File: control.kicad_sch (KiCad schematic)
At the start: 27 parts, among them J1 USB_C_Receptacle_USB2.0, J5 Conn_ARM_JTAG_SWD_10, J7 Conn_01x04_Male, U2 AMS1117-3.3, U3 STM32F042C4Tx

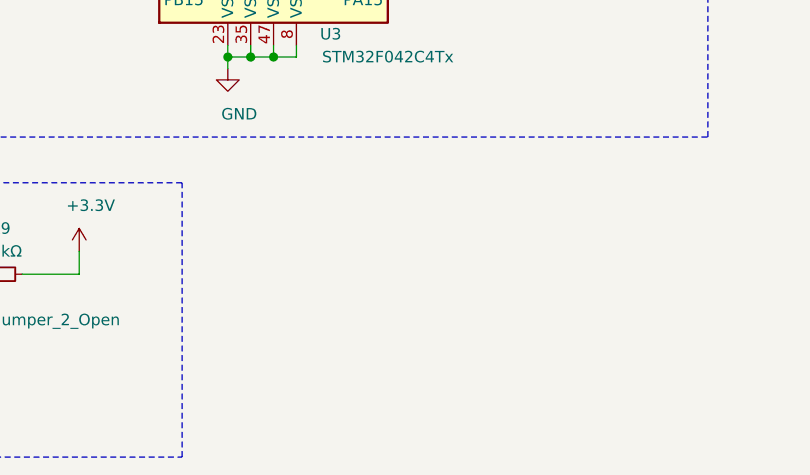
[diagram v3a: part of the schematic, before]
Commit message: fix LEDs, add power LED
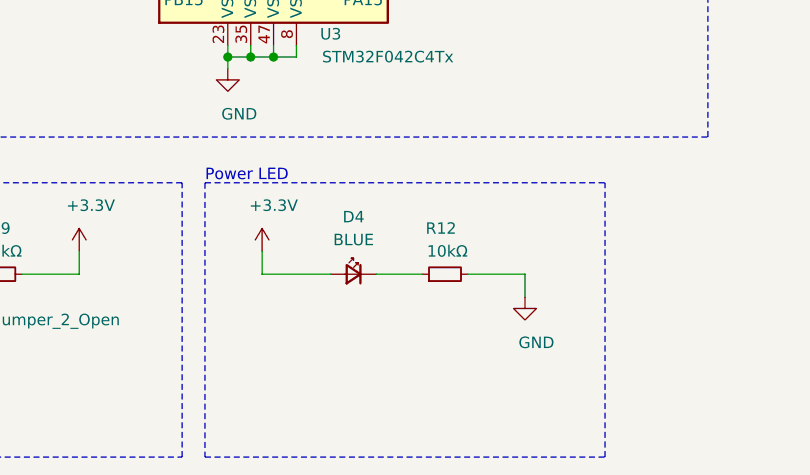
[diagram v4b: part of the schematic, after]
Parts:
- added D4: BLUE, symbol Device:LED_Small
- added R12: 10kΩ, Resistor_SMD:R_0402_1005Metric, symbol Device:R_Small
- J1: footprint (none) -> Connector_USB:USB_C_Receptacle_Amphenol_12401610E4-2A
- L1: footprint (none) -> Inductor_SMD:L_0402_1005Metric
- R1, R2: footprint (none) -> Resistor_SMD:R_0402_1005Metric
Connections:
- net +3V3: now also D4.2 (A)
- net GND: now also R12.2
- new net: D4.1 (K), R12.1
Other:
- note added: "Power LED"
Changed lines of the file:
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@@
+    (stroke (width 0) (type solid) (color 0 0 0 0))
+  )
+  (wire (pts (xy 115.57 170.18) (xy 115.57 172.72))
+    (stroke (width 0) (type solid) (color 0 0 0 0))
+  )
+  (wire (pts (xy 115.57 172.72) (xy 123.19 172.72))
     (stroke (width 0) (type solid) (color 0 0 0 0))
   )
@@
     (stroke (width 0) (type solid) (color 0 0 0 0))
   )
+  (wire (pts (xy 128.27 172.72) (xy 133.35 172.72))
+    (stroke (width 0) (type solid) (color 0 0 0 0))
+  )
   (wire (pts (xy 132.08 31.75) (xy 132.08 34.29))
     (stroke (width 0) (type solid) (color 0 0 0 0))
@@
     (stroke (width 0) (type solid) (color 0 0 0 0))
   )
+  (wire (pts (xy 138.43 172.72) (xy 144.78 172.72))
+    (stroke (width 0) (type solid) (color 0 0 0 0))
+  )
+  (wire (pts (xy 144.78 172.72) (xy 144.78 175.26))
+    (stroke (width 0) (type solid) (color 0 0 0 0))
+  )
   (wire (pts (xy 157.48 26.67) (xy 157.48 29.21))
     (stroke (width 0) (type solid) (color 0 0 0 0))
@@
     (stroke (width 0) (type dash) (color 0 0 0 0))
   )
+  (polyline (pts (xy 109.22 162.56) (xy 109.22 193.04))
+    (stroke (width 0) (type dash) (color 0 0 0 0))
+  )
+  (polyline (pts (xy 109.22 162.56) (xy 153.67 162.56))
+    (stroke (width 0) (type dash) (color 0 0 0 0))
+  )
+  (polyline (pts (xy 109.22 193.04) (xy 153.67 193.04))
+    (stroke (width 0) (type dash) (color 0 0 0 0))
+  )
   (polyline (pts (xy 147.32 17.78) (xy 147.32 52.07))
     (stroke (width 0) (type dash) (color 0 0 0 0))
@@
   )
   (polyline (pts (xy 152.4 50.8) (xy 269.24 50.8))
+    (stroke (width 0) (type dash) (color 0 0 0 0))
+  )
+  (polyline (pts (xy 153.67 193.04) (xy 153.67 162.56))
     (stroke (width 0) (type dash) (color 0 0 0 0))
   )
@@
     (effects (font (size 1.27 1.27)) (justify left bottom))
   )
+  (text "Power LED" (at 109.22 162.56 0)
+    (effects (font (size 1.27 1.27)) (justify left bottom))
+  )
   (text "Power Supply Decoupling" (at 152.4 17.78 0)
     (effects (font (size 1.27 1.27)) (justify left bottom))
@@
     (property "Reference" "L1" (id 0) (at 204.47 59.69 90))
     (property "Value" "39nH" (id 1) (at 204.47 62.23 90))
-    (property "Footprint" "" (id 2) (at 204.47 64.77 0)
+    (property "Footprint" "Inductor_SMD:L_0402_1005Metric" (id 2) (at 204.47 64.77 0)
       (effects (font (size 1.27 1.27)) hide)
     )
@@
     )
   )
+  (symbol (lib_id "power:+3.3V") (at 115.57 170.18 0) (unit 1)
+    (in_bom yes) (on_board yes)
+    (property "Reference" "#PWR032" (id 0) (at 115.57 173.99 0)
+      (effects (font (size 1.27 1.27)) hide)
+    )
+    (property "Value" "+3.3V" (id 1) (at 116.84 165.1 0))
+    (property "Footprint" "" (id 2) (at 115.57 170.18 0)
+      (effects (font (size 1.27 1.27)) hide)
+    )
+    (property "Datasheet" "" (id 3) (at 115.57 170.18 0)
+      (effects (font (size 1.27 1.27)) hide)
+    )
+  )
   (symbol (lib_id "power:+3.3VA") (at 121.92 71.12 0) (unit 1)
     (in_bom yes) (on_board yes)
@@
     )
   )
+  (symbol (lib_id "power:GND") (at 144.78 175.26 0) (unit 1)
+    (in_bom yes) (on_board yes)
+    (property "Reference" "#PWR033" (id 0) (at 144.78 181.61 0)
+      (effects (font (size 1.27 1.27)) hide)
+    )
+    (property "Value" "GND" (id 1) (at 146.05 180.34 0))
+    (property "Footprint" "" (id 2) (at 144.78 175.26 0)
+      (effects (font (size 1.27 1.27)) hide)
+    )
+    (property "Datasheet" "" (id 3) (at 144.78 175.26 0)
+      (effects (font (size 1.27 1.27)) hide)
+    )
+  )
   (symbol (lib_id "power:GND") (at 157.48 41.91 0) (unit 1)
     (in_bom yes) (on_board yes)
@@
       (effects (font (size 1.27 1.27)) (justify left))
     )
-    (property "Footprint" "" (id 2) (at 31.75 86.36 0)
+    (property "Footprint" "Resistor_SMD:R_0402_1005Metric" (id 2) (at 31.75 86.36 0)
       (effects (font (size 1.27 1.27)) hide)
     )
@@
       (effects (font (size 1.27 1.27)) (justify left))
     )
-    (property "Footprint" "" (id 2) (at 50.8 86.36 0)
+    (property "Footprint" "Resistor_SMD:R_0402_1005Metric" (id 2) (at 50.8 86.36 0)
       (effects (font (size 1.27 1.27)) hide)
     )
@@
     )
     (property "Datasheet" "~" (id 3) (at 86.36 172.72 0)
+      (effects (font (size 1.27 1.27)) hide)
+    )
+  )
+  (symbol (lib_id "Device:R_Small") (at 135.89 172.72 90) (unit 1)
+    (in_bom yes) (on_board yes)
+    (property "Reference" "R12" (id 0) (at 137.16 167.64 90)
+      (effects (font (size 1.27 1.27)) (justify left))
+    )
+    (property "Value" "10kΩ" (id 1) (at 138.43 170.18 90)
+      (effects (font (size 1.27 1.27)) (justify left))
+    )
+    (property "Footprint" "Resistor_SMD:R_0402_1005Metric" (id 2) (at 135.89 172.72 0)
+      (effects (font (size 1.27 1.27)) hide)
+    )
+    (property "Datasheet" "~" (id 3) (at 135.89 172.72 0)
       (effects (font (size 1.27 1.27)) hide)
     )
@@
     )
   )
+  (symbol (lib_id "Device:LED_Small") (at 125.73 172.72 0) (mirror y) (unit 1)
+    (in_bom yes) (on_board yes)
+    (property "Reference" "D4" (id 0) (at 125.73 166.37 0))
+    (property "Value" "BLUE" (id 1) (at 125.73 168.91 0))
+    (property "Footprint" "" (id 2) (at 125.73 172.72 90)
+      (effects (font (size 1.27 1.27)) hide)
+    )
+    (property "Datasheet" "~" (id 3) (at 125.73 172.72 90)
+      (effects (font (size 1.27 1.27)) hide)
+    )
+  )
   (symbol (lib_id "Device:C_Small") (at 106.68 36.83 0) (unit 1)
     (in_bom yes) (on_board yes)
@@
     (property "Reference" "J1" (id 0) (at 35.56 21.59 0))
     (property "Value" "USB_C_Receptacle_USB2.0" (id 1) (at 35.56 24.13 0))
-    (property "Footprint" "" (id 2) (at 35.56 44.45 0)
-      (effects (font (size 1.27 1.27)) hide)
-    )
+    (property "Footprint" "Connector_USB:USB_C_Receptacle_Amphenol_12401610E4-2A" (id 2) (at 35.56 44.45 0)
+      (effects (font (size 1.27 1.27)) hide)
+    )

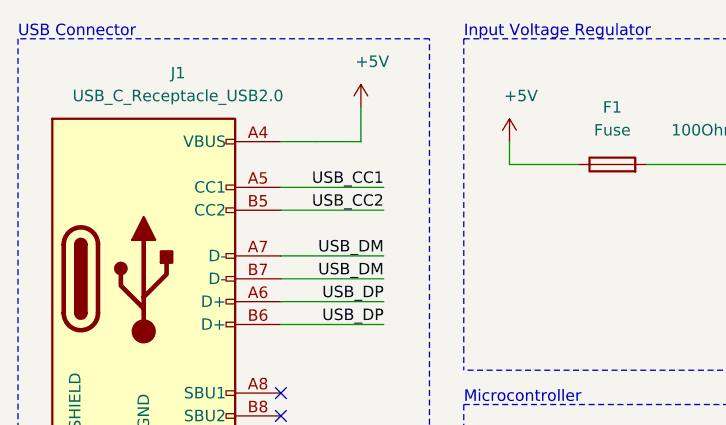
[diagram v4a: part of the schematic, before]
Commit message: add voltage measurement
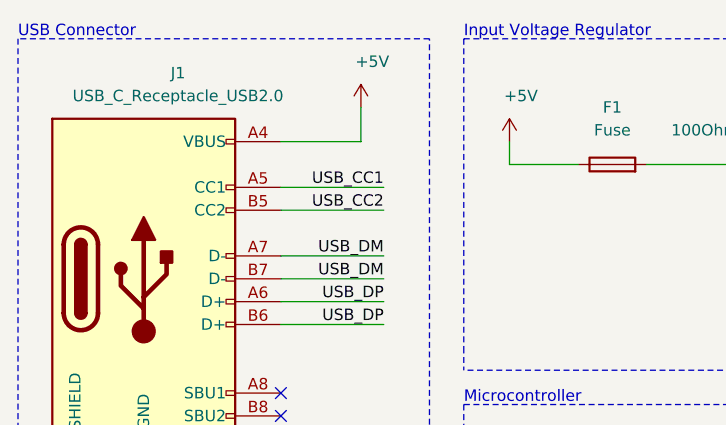
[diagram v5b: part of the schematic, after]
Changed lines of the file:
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@@
   (junction (at 227.33 29.21) (diameter 1.016) (color 0 0 0 0))
   (junction (at 227.33 39.37) (diameter 1.016) (color 0 0 0 0))
-  (no_connect (at 46.99 57.15))
   (no_connect (at 46.99 59.69))
   (no_connect (at 24.13 67.31))
+  (no_connect (at 46.99 57.15))
   (wire (pts (xy 22.86 81.28) (xy 31.75 81.28))
     (stroke (width 0) (type solid) (color 0 0 0 0))
@@
     (stroke (width 0) (type solid) (color 0 0 0 0))
   )
+  (wire (pts (xy 46.99 29.21) (xy 55.88 29.21))
+    (stroke (width 0) (type solid) (color 0 0 0 0))
+  )
   (wire (pts (xy 46.99 34.29) (xy 58.42 34.29))
     (stroke (width 0) (type solid) (color 0 0 0 0))
@@
     (stroke (width 0) (type solid) (color 0 0 0 0))
   )
-  (wire (pts (xy 50.8 29.21) (xy 46.99 29.21))
-    (stroke (width 0) (type solid) (color 0 0 0 0))
-  )
-  (wire (pts (xy 50.8 29.21) (xy 55.88 29.21))
-    (stroke (width 0) (type solid) (color 0 0 0 0))
-  )

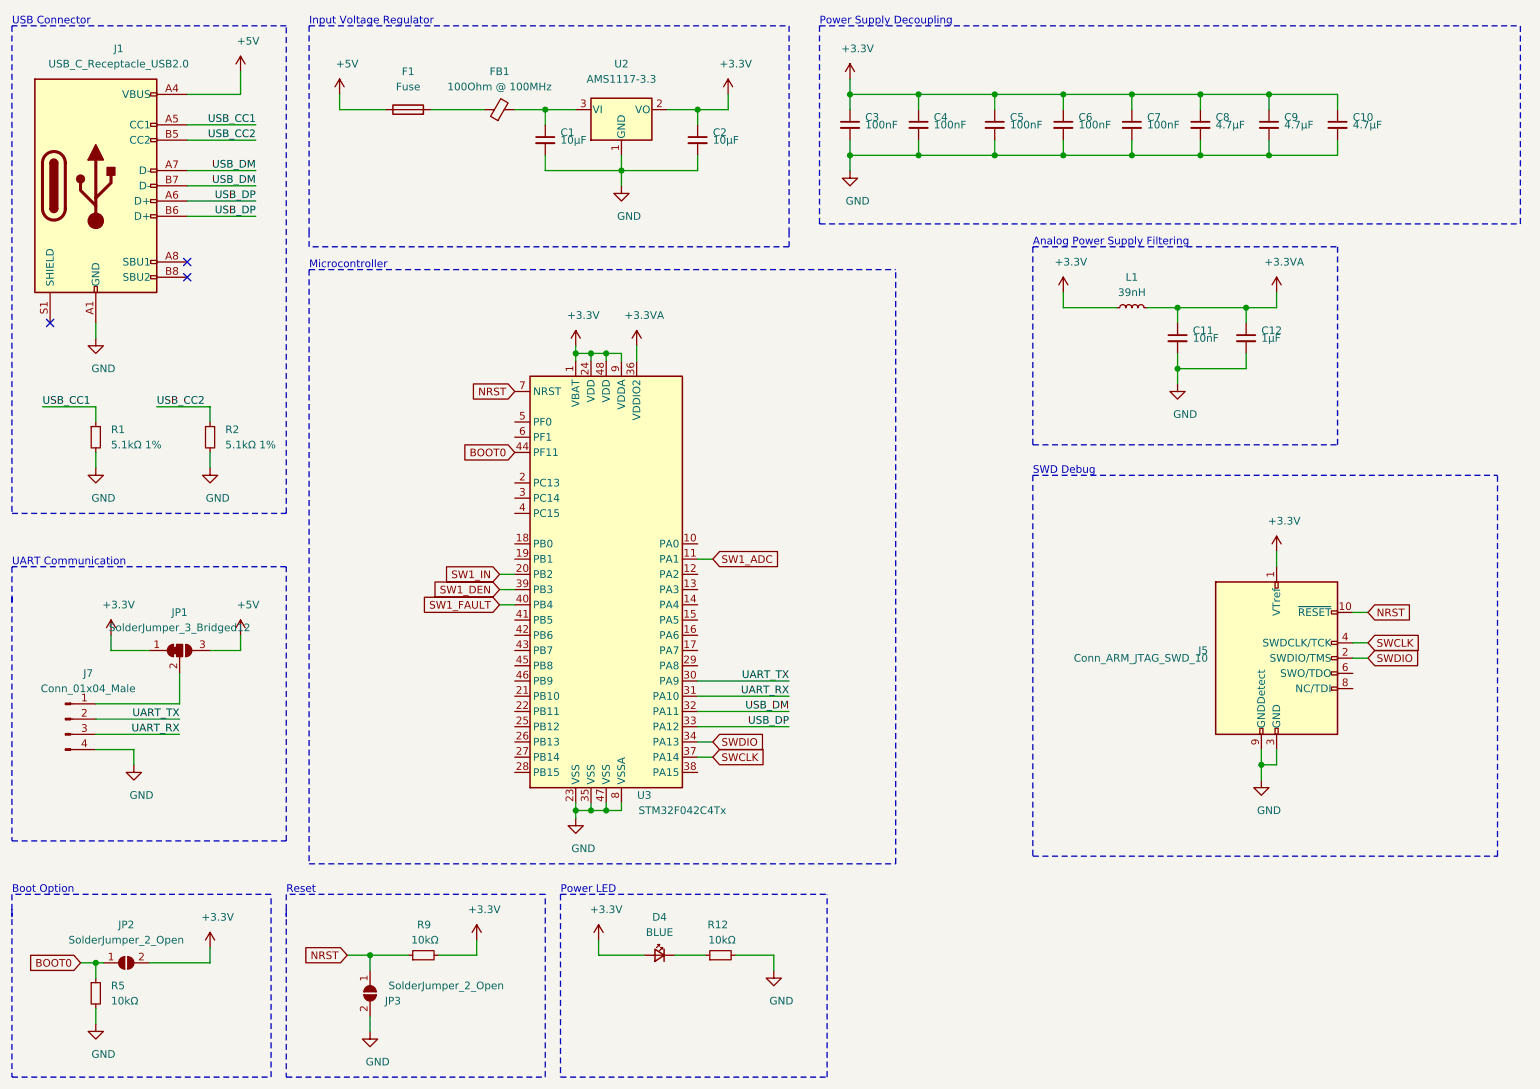
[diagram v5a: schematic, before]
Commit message: introduce hierarchical sheets for power switches
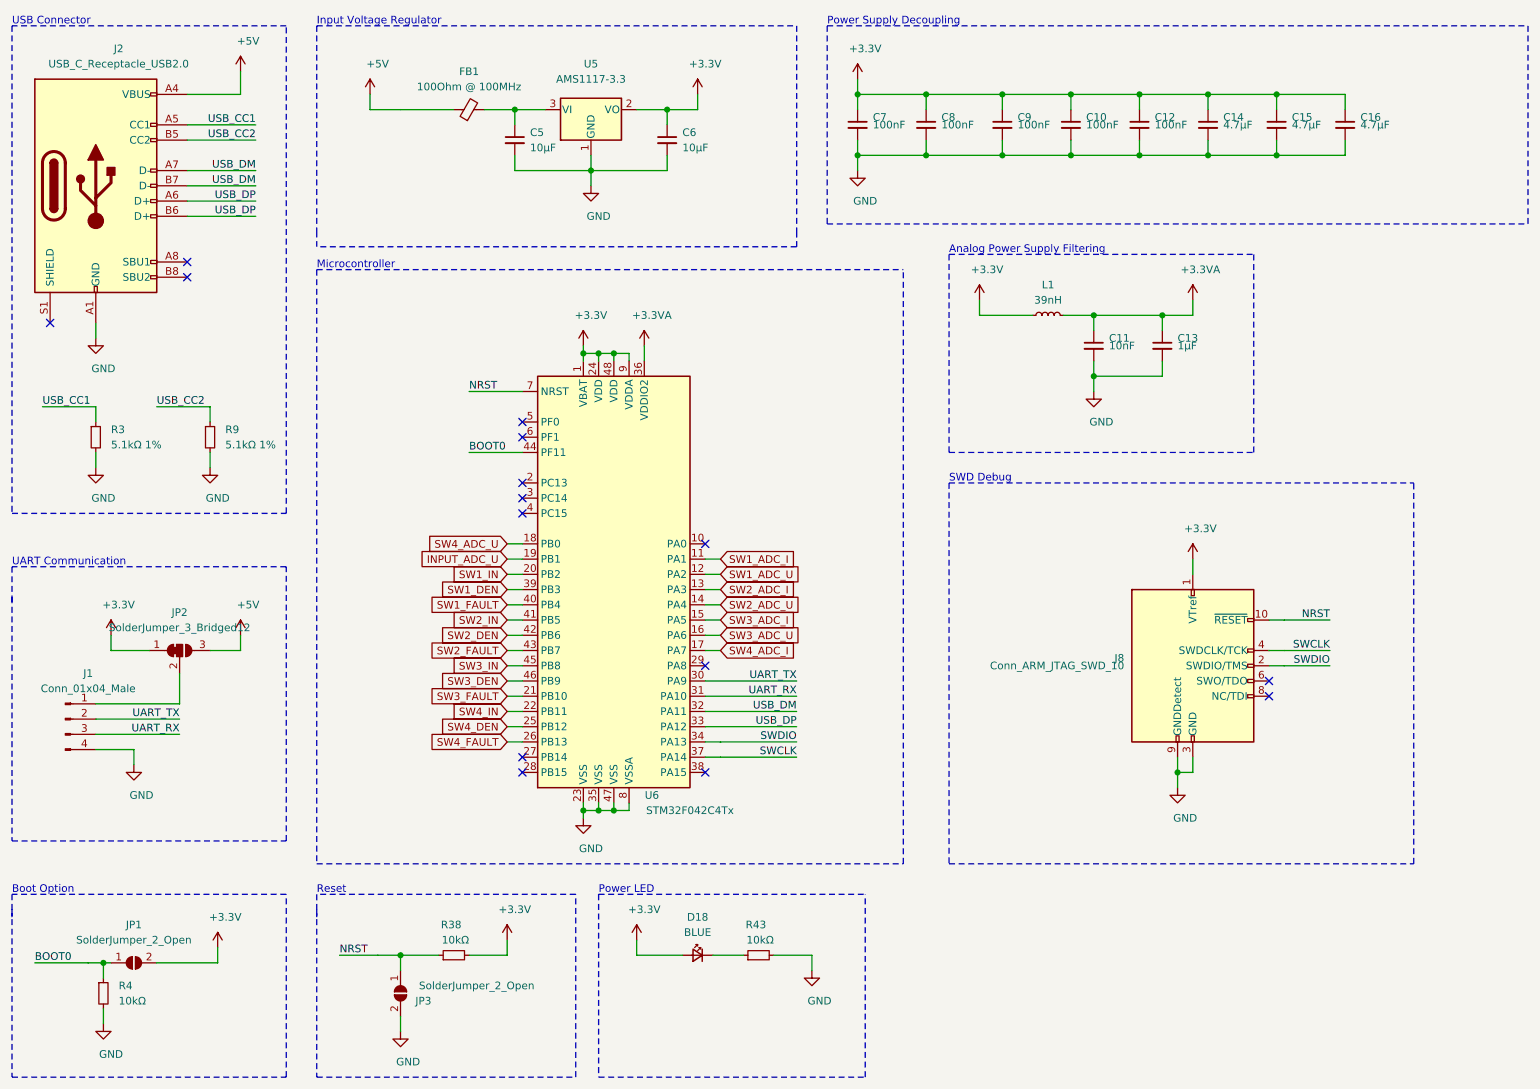
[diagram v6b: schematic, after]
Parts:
- removed F1: Fuse, symbol Device:Fuse
- C10: renamed from C6; footprint Capacitor_SMD:C_0402_1005Metric -> Capacitor_SMD:C_0603_1608Metric
- C11: footprint Capacitor_SMD:C_0402_1005Metric -> Capacitor_SMD:C_0603_1608Metric
- C12: renamed from C7; footprint Capacitor_SMD:C_0402_1005Metric -> Capacitor_SMD:C_0603_1608Metric
- C13: renamed from C12; footprint Capacitor_SMD:C_0402_1005Metric -> Capacitor_SMD:C_0603_1608Metric
- C14: renamed from C8; footprint Capacitor_SMD:C_0402_1005Metric -> Capacitor_SMD:C_0603_1608Metric
- C15: renamed from C9; footprint Capacitor_SMD:C_0402_1005Metric -> Capacitor_SMD:C_0603_1608Metric
- C16: renamed from C10; footprint Capacitor_SMD:C_0402_1005Metric -> Capacitor_SMD:C_0603_1608Metric
- C5: renamed from C1; footprint Capacitor_SMD:C_0402_1005Metric -> Capacitor_SMD:C_0603_1608Metric
- C6: renamed from C2; footprint Capacitor_SMD:C_0402_1005Metric -> Capacitor_SMD:C_0603_1608Metric
- C7: renamed from C3; footprint Capacitor_SMD:C_0402_1005Metric -> Capacitor_SMD:C_0603_1608Metric
- C8: renamed from C4; footprint Capacitor_SMD:C_0402_1005Metric -> Capacitor_SMD:C_0603_1608Metric
- C9: renamed from C5; footprint Capacitor_SMD:C_0402_1005Metric -> Capacitor_SMD:C_0603_1608Metric
- D18: renamed from D4; footprint (none) -> LED_SMD:LED_0603_1608Metric
- FB1: footprint (none) -> Inductor_SMD:L_0805_2012Metric
- L1: footprint Inductor_SMD:L_0402_1005Metric -> Inductor_SMD:L_0603_1608Metric
- R3: renamed from R1; footprint Resistor_SMD:R_0402_1005Metric -> Resistor_SMD:R_0603_1608Metric
- R38: renamed from R9; footprint Resistor_SMD:R_0402_1005Metric -> Resistor_SMD:R_0603_1608Metric
- R4: renamed from R5; footprint Resistor_SMD:R_0402_1005Metric -> Resistor_SMD:R_0603_1608Metric
- R43: renamed from R12; footprint Resistor_SMD:R_0402_1005Metric -> Resistor_SMD:R_0603_1608Metric
- R9: renamed from R2; footprint Resistor_SMD:R_0402_1005Metric -> Resistor_SMD:R_0603_1608Metric
- renumbered J7 to J1, J1 to J2, J5 to J8, JP2 to JP1, JP1 to JP2, U2 to U5, U3 to U6
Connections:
- net +5V: now also FB1.1
- net SW1_ADC_U: now reaches U6.12 (PA2)
- net SW2_ADC_I: now reaches U6.13 (PA3)
- net SW2_ADC_U: now reaches U6.14 (PA4)
- net SW3_ADC_I: now reaches U6.15 (PA5)
- net SW3_ADC_U: now reaches U6.16 (PA6)
- net SW4_ADC_I: now reaches U6.17 (PA7)
- net SW4_ADC_U: now reaches U6.18 (PB0)
- net INPUT_ADC_U: now reaches U6.19 (PB1)
- net SW3_FAULT: now reaches U6.21 (PB10)
- net SW4_IN: now reaches U6.22 (PB11)
- net SW4_DEN: now reaches U6.25 (PB12)
- net SW4_FAULT: now reaches U6.26 (PB13)
- net SW2_IN: now reaches U6.41 (PB5)
- net SW2_DEN: now reaches U6.42 (PB6)
- net SW2_FAULT: now reaches U6.43 (PB7)
- net SW3_IN: now reaches U6.45 (PB8)
- net SW3_DEN: now reaches U6.46 (PB9)
- net SW1_ADC renamed SW1_ADC_I
- no-connect marks 3 -> 15
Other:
- moved on the sheet: C10, C11, C12, C13, C14, C15, C16, C5, C6, C7, C8, C9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

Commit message: initial component placement
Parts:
- renumbered J2 to J7, J1 to J8, J8 to J9, JP2 to JP8
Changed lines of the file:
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@@
   (page 1 7)
   (paper "A4")
+  (title_block
+    (comment 4 "Author: Stefan Agner")
+  )
   (junction (at 33.02 173.99) (diameter 1.016) (color 0 0 0 0))
   (junction (at 82.55 172.72) (diameter 1.016) (color 0 0 0 0))
@@
   (symbol (lib_id "Connector:Conn_01x04_Male") (at 26.67 133.35 0) (unit 1)
     (in_bom yes) (on_board yes)
-    (property "Reference" "J1" (id 0) (at 30.48 125.73 0))
+    (property "Reference" "J8" (id 0) (at 30.48 125.73 0))
     (property "Value" "Conn_01x04_Male" (id 1) (at 30.48 128.27 0))
     (property "Footprint" "Connector_PinHeader_2.54mm:PinHeader_1x04_P2.54mm_Vertical" (id 2) (at 26.67 133.35 0)
@@
   (symbol (lib_id "Jumper:SolderJumper_3_Bridged12") (at 45.72 121.92 0) (unit 1)
     (in_bom yes) (on_board yes)
-    (property "Reference" "JP2" (id 0) (at 45.72 115.57 0))
+    (property "Reference" "JP8" (id 0) (at 45.72 115.57 0))
     (property "Value" "SolderJumper_3_Bridged12" (id 1) (at 45.72 118.11 0))
     (property "Footprint" "Jumper:SolderJumper-3_P1.3mm_Bridged12_RoundedPad1.0x1.5mm_NumberLabels" (id 2) (at 45.72 121.92 0)
@@
   (symbol (lib_id "Connector:Conn_ARM_JTAG_SWD_10") (at 214.63 124.46 0) (unit 1)
     (in_bom yes) (on_board yes)
-    (property "Reference" "J8" (id 0) (at 203.2 123.19 0)
+    (property "Reference" "J9" (id 0) (at 203.2 123.19 0)
       (effects (font (size 1.27 1.27)) (justify right))
     )
@@
   (symbol (lib_id "Connector:USB_C_Receptacle_USB2.0") (at 31.75 44.45 0) (unit 1)
     (in_bom yes) (on_board yes)
-    (property "Reference" "J2" (id 0) (at 35.56 21.59 0))
+    (property "Reference" "J7" (id 0) (at 35.56 21.59 0))
     (property "Value" "USB_C_Receptacle_USB2.0" (id 1) (at 35.56 24.13 0))
     (property "Footprint" "Connector_USB:USB_C_Receptacle_Amphenol_12401610E4-2A" (id 2) (at 35.56 44.45 0)
